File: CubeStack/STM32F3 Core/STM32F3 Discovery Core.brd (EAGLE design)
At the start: 63.5 x 76.2 mm, 46 parts, among them IC1 FT230XQ, Q1 FC-12M, Q2 MBT3904DW2T1, Q3 MBT3904DW2T1

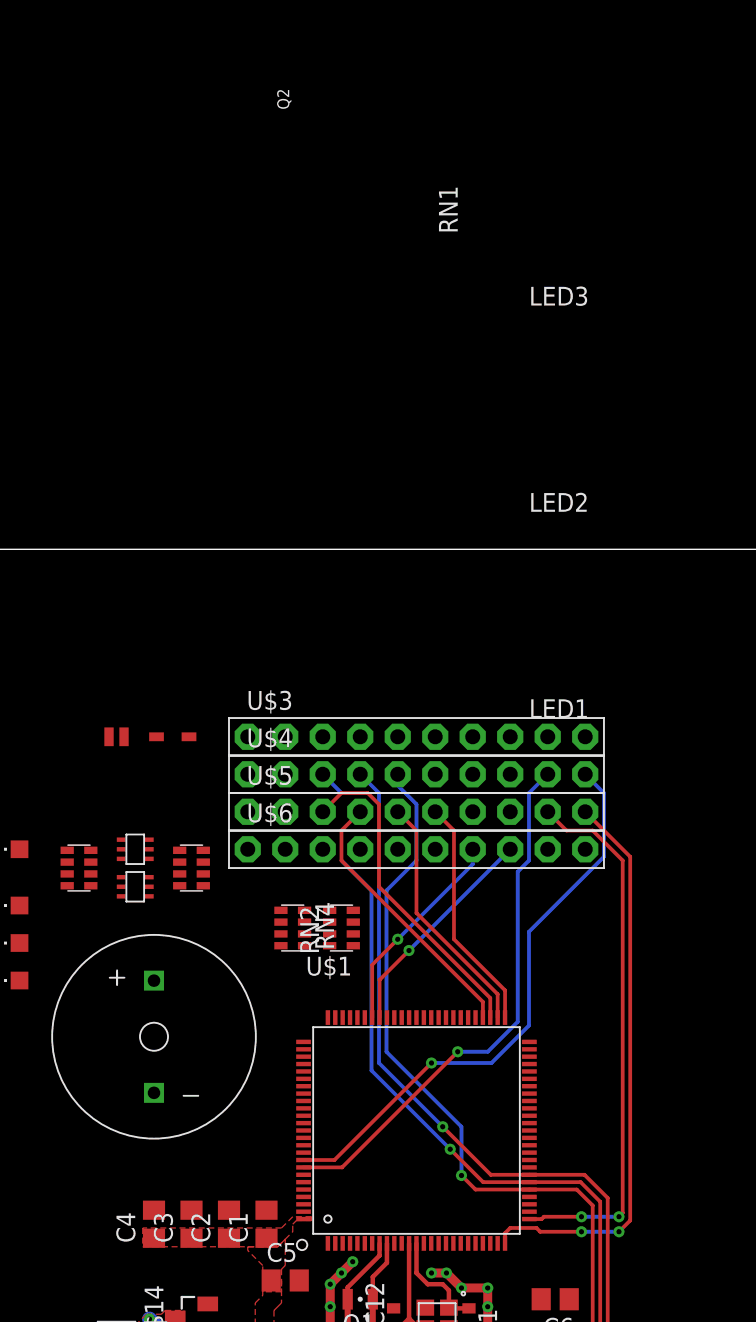
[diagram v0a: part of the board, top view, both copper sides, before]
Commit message: Routed PWM, GPIO lines
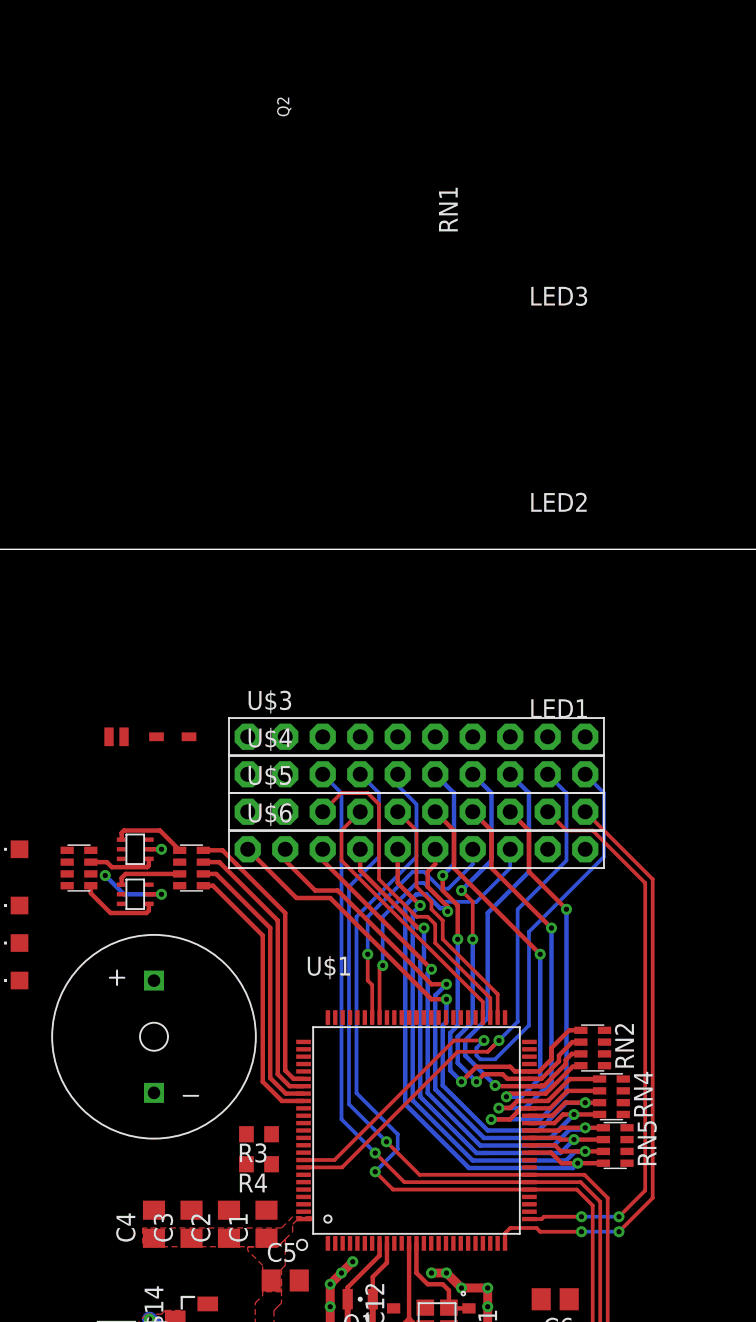
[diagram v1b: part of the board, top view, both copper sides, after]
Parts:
- added R3, R4: (no value), resistor:R0603
- added RN5: 4.7K, resistor-net:CTS742C083
- moved RN4 24.4 mm to (45.0, 39.1)
- moved RN2 18.9 mm to (43.7, 42.4), turned to 270 degrees
- moved Q2 0.51 mm to (12.7, 52.8)
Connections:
- net N$8 renamed L_3_G
- removed net D11: RN3.1
- removed net D12: RN3.2
- removed net D13: RN3.4
- removed net N$12: U$7.2
- removed net N$13: RN2.2
- removed net N$14: RN2.3
- removed net N$15: RN2.4
- removed net N$16: RN4.1
- removed net N$17: RN4.2
- removed net N$18: RN4.3
- removed net N$19: RN4.4
- removed net N$35: U$6.1
- removed net N$36: U$6.2
- removed net N$37: U$6.3
- removed net N$38: U$6.4
- removed net N$39: U$6.5
- removed net N$40: U$6.6
- removed net N$9: RN2.1
- removed net PWM6/D45: RN3.3
- new net FLASH_CS: U$1.P$51
- new net LED1: RN3.1, U$1.P$84
- new net LED2: RN3.2, U$1.P$83
- new net LED3: RN3.3, U$1.P$82
- new net LS: RN3.4, U$1.P$81
- new net N$25: RN2.6
- new net N$26: RN2.7
- new net PWM0: RN4.3, U$1.P$40, U$6.1
- new net PWM1: RN4.4, U$1.P$39, U$6.2
- new net PWM2: RN5.1, U$1.P$38, U$6.3
- new net PWM3: RN5.2, U$1.P$37, U$6.4
- new net PWM4: RN5.3, U$1.P$36, U$6.5
- new net PWM5: RN5.4, U$1.P$35, U$6.6
- net 3.3V: now also R3.2, RN5.5, RN5.6, RN5.7, RN5.8; no longer RN2.6, RN2.7
- net GND: now also R4.2
- net N$20: now also R3.1, R4.1
- net SD_CS: now also U$7.2
- net SPI0CS0: now also RN2.1, U$1.P$46
- net SPI0CS1: now also RN2.2, U$1.P$45
- net SPI0CS2: now also RN2.3, U$1.P$44
- net SPI1CS0: now also RN2.4, U$1.P$43; no longer U$1.P$51
- net SPI1CS1: now also RN4.1, U$1.P$42
- net SPI1CS2: now also RN4.2, U$1.P$41
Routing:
- net PWM5: track 0.00 -> 41.0 mm, vias 0 -> 2
- net PWM0: track 0.00 -> 40.4 mm, vias 0 -> 2
- net PWM1: track 0.00 -> 39.0 mm, vias 0 -> 2
- net PWM2: track 0.00 -> 38.2 mm, vias 0 -> 2
- net PWM4: track 0.00 -> 36.7 mm, vias 0 -> 2
- net PWM3: track 0.00 -> 36.3 mm, vias 0 -> 2
- net SPI1CS2: track 0.00 -> 34.7 mm, vias 0 -> 2
- net SPI0CS0: track 0.00 -> 32.9 mm, vias 0 -> 3
- net SPI1CS1: track 0.00 -> 32.4 mm, vias 0 -> 2
- net SPI0CS1: track 0.00 -> 32.1 mm, vias 0 -> 3
- net SPI0CS2: track 0.00 -> 31.7 mm, vias 0 -> 1
- net LS: track 0.00 -> 19.5 mm
- net LED3: track 0.00 -> 19.2 mm
- net LED2: track 0.00 -> 18.9 mm
- net LED1: track 0.00 -> 18.6 mm
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
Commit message: Completed STM32 Core to be Reviewed
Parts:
- added C15: (no value), resistor:C0402
- added R5: (no value), resistor:R0603
- added U1: SST26VF064B, CPSS_IC:SOIJ
- moved C8 12.3 mm to (42.7, 19.6), turned to 270 degrees
- moved RN2 1.52 mm to (45.2, 42.4)
- moved C6 1.37 mm to (41.7, 24.1)
- moved U$2 1.05 mm to (40.4, 20.1)
- moved C7 0.92 mm to (41.7, 22.1)
- moved RN4 0.25 mm to (45.2, 39.1)
- moved Q2 0.25 mm to (12.4, 52.8)
- moved Q3 0.25 mm to (12.4, 55.9)
- moved SJ1 0.25 mm to (11.7, 63.5)
- moved RN1 0.15 mm to (8.74, 54.6)
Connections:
- net RX0 renamed RX1
- net TX0 renamed TX1
- removed net N$25: RN2.6
- removed net N$26: RN2.7
- removed net RXD1: U$5.1
- removed net TXD1: U$5.2
- new net FLASH_HOLD: R5.2, U$1.P$51, U1.P$7
- new net FLASH_WP: U$1.P$47, U1.P$3
- new net RXD3: U$1.P$56, U$5.1
- new net TXD3: U$1.P$55, U$5.2
- net 3.3V: now also C15.1, R5.1, RN2.6, RN2.7, U1.P$8
- net FLASH_CS: now also U$1.P$48, U1.P$1; no longer U$1.P$51
- net GND: now also C15.2, U1.P$4
- net MISO1: now also U1.P$2
- net MOSI1: now also U1.P$5
- net SCK1: now also U1.P$6
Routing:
- net 3.3V: track 0.00 -> 364.0 mm, vias 0 -> 14
- net RX1: track 0.00 -> 87.4 mm, vias 0 -> 3
- net TX1: track 0.00 -> 84.0 mm, vias 0 -> 3
- net SWDIO: track 0.00 -> 61.4 mm, vias 0 -> 1
- net SWDCLK: track 0.00 -> 56.7 mm, vias 0 -> 1
- net SWO: track 0.00 -> 54.5 mm, vias 0 -> 1
- net 5V: track 0.00 -> 54.1 mm, vias 0 -> 3
- net RESET: track 0.00 -> 52.3 mm, vias 0 -> 1
- net GND: track 28.0 -> 77.0 mm, vias 21 -> 178
- net D+M: track 0.00 -> 46.8 mm, vias 0 -> 2
- net D-M: track 0.00 -> 42.9 mm, vias 0 -> 2
- net SD_CS: track 0.00 -> 33.5 mm, vias 0 -> 2
- net 3.3V_USB: track 6.59 -> 36.9 mm, vias 0 -> 2
- net HV: track 0.00 -> 30.2 mm, vias 0 -> 1
- net TXD3: track 0.00 -> 30.1 mm, vias 0 -> 1
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- added copper zone on layer 1, net GND
- added copper zone on layer 16, net GND
- added copper zone on layer 1, net LS_D
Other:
- board text added: "LS ENABLE"
- board text added: "MICROSD"
- board text added: "RESET"

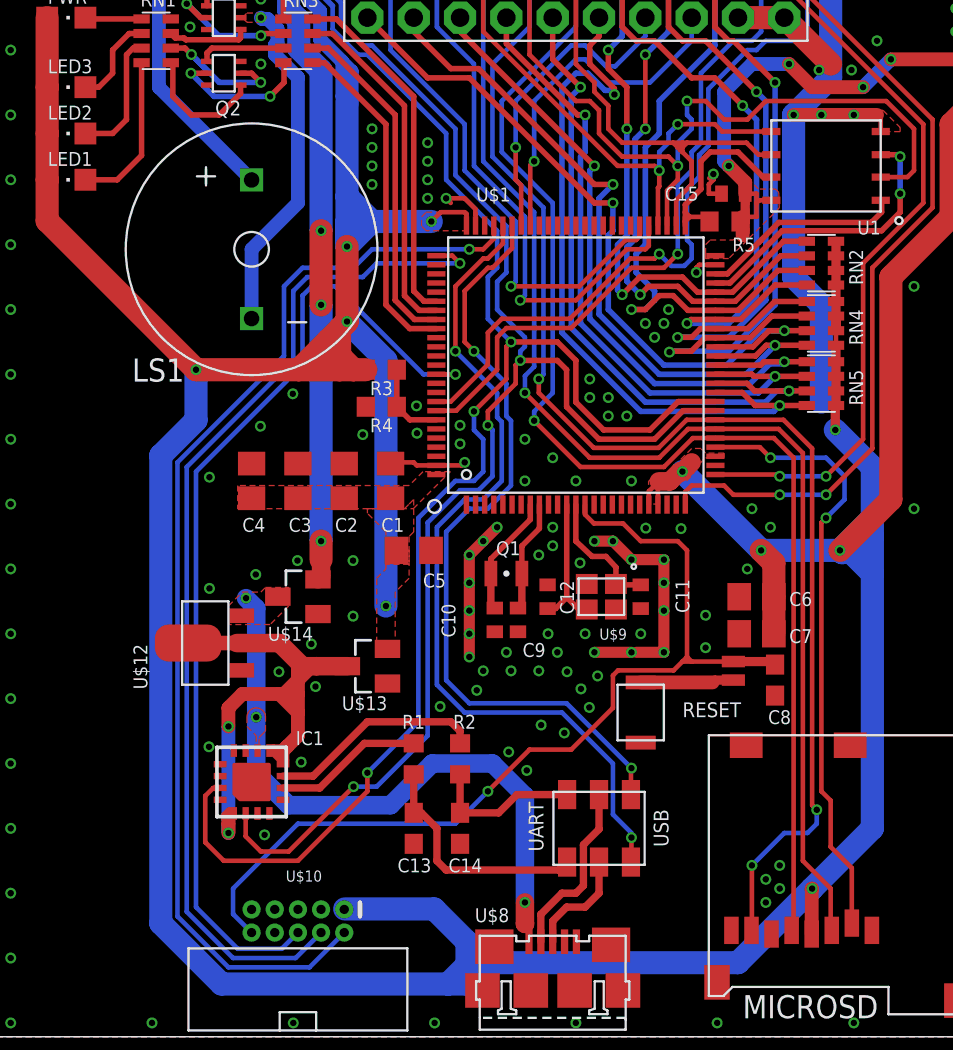
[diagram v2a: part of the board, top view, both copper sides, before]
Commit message: Added Via Stitching to Perimeter + Bus Pin Numbers
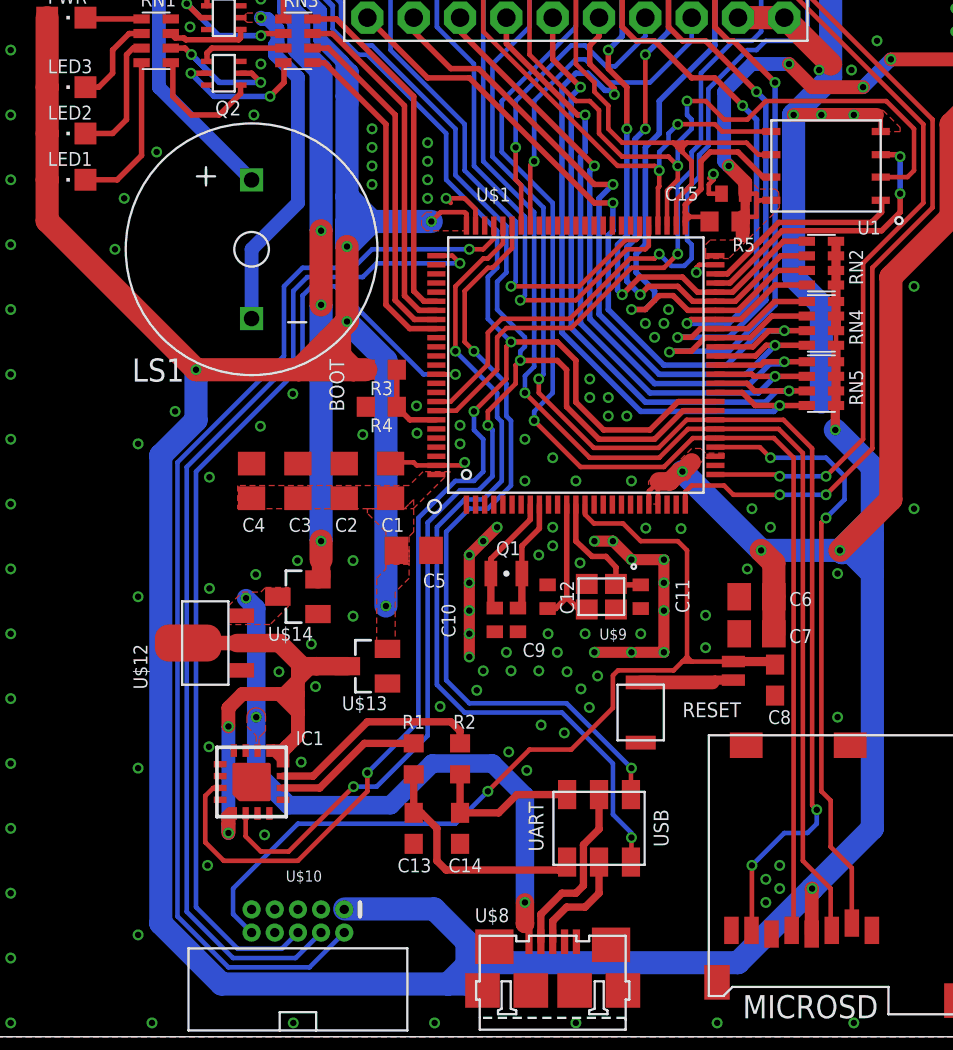
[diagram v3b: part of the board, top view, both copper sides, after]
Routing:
- net GND: vias 178 -> 190
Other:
- board text added: "BOOT"
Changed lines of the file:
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@@
 <wire x1="24.13" y1="15.748" x2="23.876" y2="16.002" width="0.254" layer="42"/>
 <wire x1="23.876" y1="16.002" x2="23.876" y2="16.256" width="0.254" layer="42"/>
+<text x="19.05" y="34.29" size="0.8128" layer="25" rot="R90">BOOT</text>
 </plain>
 <attributes>
@@
 <via x="0.762" y="36.322" extent="1-16" drill="0.35"/>
 <via x="0.762" y="39.878" extent="1-16" drill="0.35"/>
+<via x="7.747" y="5.588" extent="1-16" drill="0.35"/>
+<via x="7.747" y="32.512" extent="1-16" drill="0.35"/>
+<via x="9.779" y="34.29" extent="1-16" drill="0.35"/>
+<via x="7.747" y="24.13" extent="1-16" drill="0.35"/>
+<via x="7.747" y="14.732" extent="1-16" drill="0.35"/>
+<via x="14.097" y="50.546" extent="1-16" drill="0.35"/>
+<via x="8.763" y="48.514" extent="1-16" drill="0.35"/>
+<via x="6.985" y="45.974" extent="1-16" drill="0.35"/>
+<via x="6.477" y="43.18" extent="1-16" drill="0.35"/>
+<via x="11.557" y="9.398" extent="1-16" drill="0.35"/>
+<via x="46.101" y="25.4" extent="1-16" drill="0.35"/>
+<via x="46.101" y="17.526" extent="1-16" drill="0.35"/>
 </signal>
 <signal name="RESET">

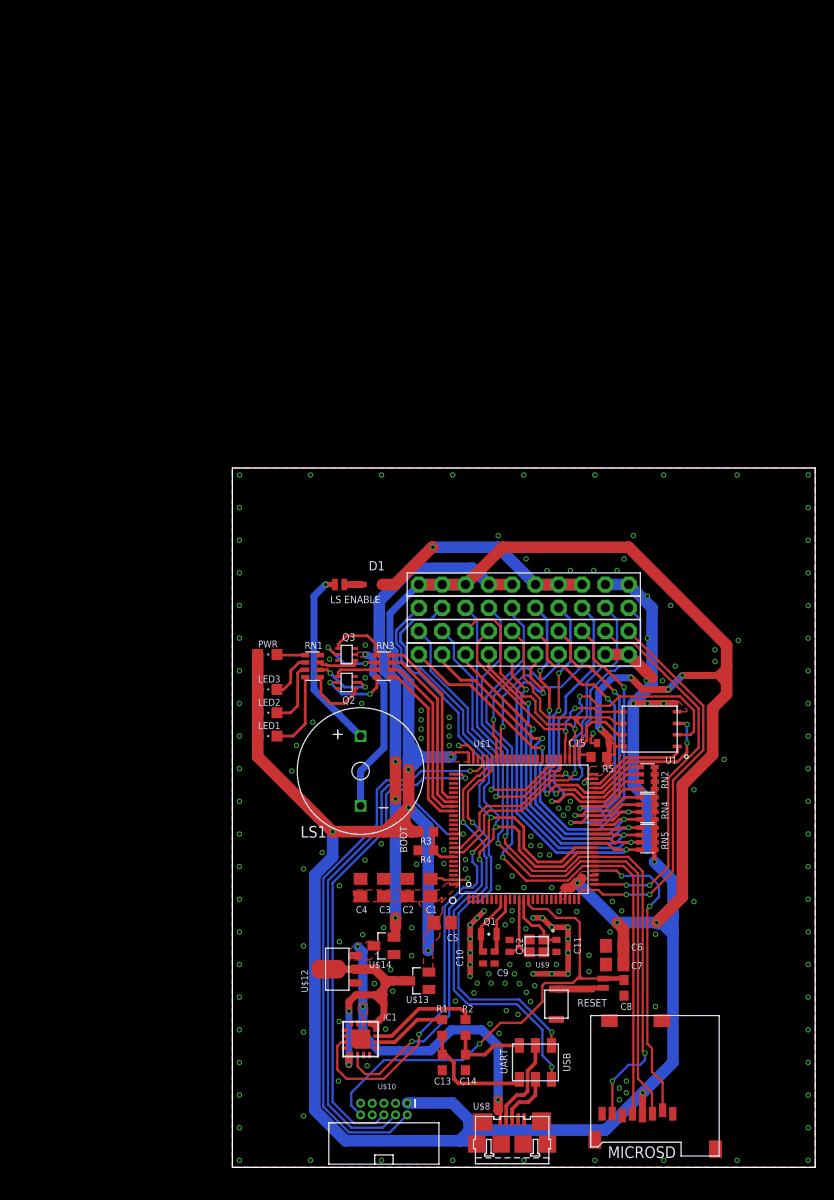
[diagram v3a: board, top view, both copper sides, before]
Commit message: Update component names
TODO: Change Resistor/Capacitor names
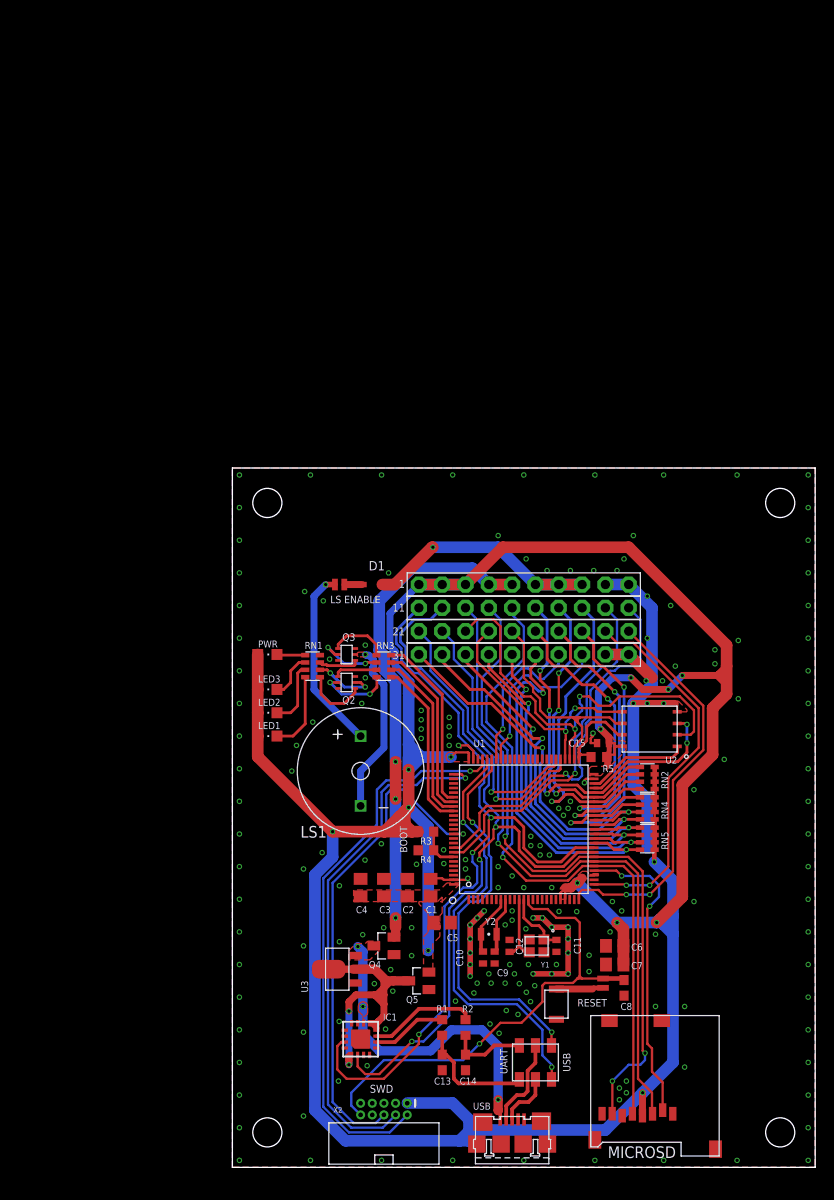
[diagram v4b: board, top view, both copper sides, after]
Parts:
- removed U$1: STM32F303-VCT6, CPSS_CPU:LQFP-100
- added U2: SST26VF064B, CPSS_IC:SOIJ
- U1: value SST26VF064B -> STM32F303-VCT6; device CPSS_IC:SOIJ -> CPSS_CPU:LQFP-100
- moved U1 17.5 mm to (31.8, 36.8), turned to 0 degrees
- renumbered Q1 to Y2, U$10 to X2, U$11 to SW2, U$12 to U3, U$13 to Q5, U$14 to Q4, U$2 to SJ2, U$3 to X1A, U$4 to X1B, U$5 to X1C, U$6 to X1D, U$7 to SD1, U$8 to USB, U$9 to Y1
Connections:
- net 3.3V: now also U1.P$100, U1.P$21, U1.P$22, U1.P$28, U1.P$50, U1.P$75, U2.P$8; no longer U$1.P$100, U$1.P$21, U$1.P$22, U$1.P$28, U$1.P$50, U$1.P$75, U1.P$8
- net D+M: now also U1.P$71; no longer U$1.P$71
- net D-M: now also U1.P$70; no longer U$1.P$70
- net FLASH_CS: now also U1.P$48, U2.P$1; no longer U$1.P$48, U1.P$1
- net FLASH_HOLD: now also U1.P$51, U2.P$7; no longer U$1.P$51, U1.P$7
- net FLASH_WP: now also U1.P$47, U2.P$3; no longer U$1.P$47, U1.P$3
- net GND: now also U1.P$20, U1.P$49, U1.P$74, U1.P$99, U2.P$4; no longer U$1.P$20, U$1.P$49, U$1.P$74, U$1.P$99, U1.P$4
- net LED1: now also U1.P$84; no longer U$1.P$84
- net LED2: now also U1.P$83; no longer U$1.P$83
- net LED3: now also U1.P$82; no longer U$1.P$82
- net LS: now also U1.P$81; no longer U$1.P$81
- net MISO0: now also U1.P$31; no longer U$1.P$31
- net MISO1: now also U1.P$53, U2.P$2; no longer U$1.P$53, U1.P$2
- net MOSI0: now also U1.P$32; no longer U$1.P$32
- net MOSI1: now also U1.P$54, U2.P$5; no longer U$1.P$54, U1.P$5
- net N$2: now also U1.P$8; no longer U$1.P$8
- net N$20: now also U1.P$94; no longer U$1.P$94
- net N$4: now also U1.P$9; no longer U$1.P$9
- net N$5: now also U1.P$12; no longer U$1.P$12
- net N$6: now also U1.P$13; no longer U$1.P$13
- net PWM0: now also U1.P$40; no longer U$1.P$40
- net PWM1: now also U1.P$39; no longer U$1.P$39
- net PWM2: now also U1.P$38; no longer U$1.P$38
- net PWM3: now also U1.P$37; no longer U$1.P$37
- net PWM4: now also U1.P$36; no longer U$1.P$36
- net PWM5: now also U1.P$35; no longer U$1.P$35
- net RESET: now also U1.P$14; no longer U$1.P$14
- net RX1: now also U1.P$34; no longer U$1.P$34
- net RXD2: now also U1.P$26; no longer U$1.P$26
- net RXD3: now also U1.P$56; no longer U$1.P$56
- net SCK0: now also U1.P$30; no longer U$1.P$30
- net SCK1: now also U1.P$52, U2.P$6; no longer U$1.P$52, U1.P$6
- net SCL0: now also U1.P$92; no longer U$1.P$92
- net SCL1: now also U1.P$68; no longer U$1.P$68
- net SDA0: now also U1.P$93; no longer U$1.P$93
- net SDA1: now also U1.P$69; no longer U$1.P$69
- net SD_CS: now also U1.P$29; no longer U$1.P$29
- net SPI0CS0: now also U1.P$46; no longer U$1.P$46
- net SPI0CS1: now also U1.P$45; no longer U$1.P$45
- net SPI0CS2: now also U1.P$44; no longer U$1.P$44
- net SPI1CS0: now also U1.P$43; no longer U$1.P$43
- net SPI1CS1: now also U1.P$42; no longer U$1.P$42
- net SPI1CS2: now also U1.P$41; no longer U$1.P$41
- net SWDCLK: now also U1.P$76; no longer U$1.P$76
- net SWDIO: now also U1.P$72; no longer U$1.P$72
- net SWO: now also U1.P$89; no longer U$1.P$89
- net TX1: now also U1.P$33; no longer U$1.P$33
- net TXD2: now also U1.P$25; no longer U$1.P$25
- net TXD3: now also U1.P$55; no longer U$1.P$55
- net VBAT: now also U1.P$6; no longer U$1.P$6
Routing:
- net GND: vias 190 -> 196
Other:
- board text added: "1 11 21 31"
- board text added: "SWD"
